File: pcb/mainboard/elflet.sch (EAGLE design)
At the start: 37 parts, among them J1 ZX62-B-5PA(33), J2 2212S-10SG-36, J3 STD-PINHD-1X6, Q1 IRLML6344TRPBF, Q2 ALS-PT19-315C/L177/TR8, SW1 SKRPACE010, U1 ESP-WROOM-32, U2 ADP3338AKCZ-3.3, U3 OSRB38C9AA, U4 BME280

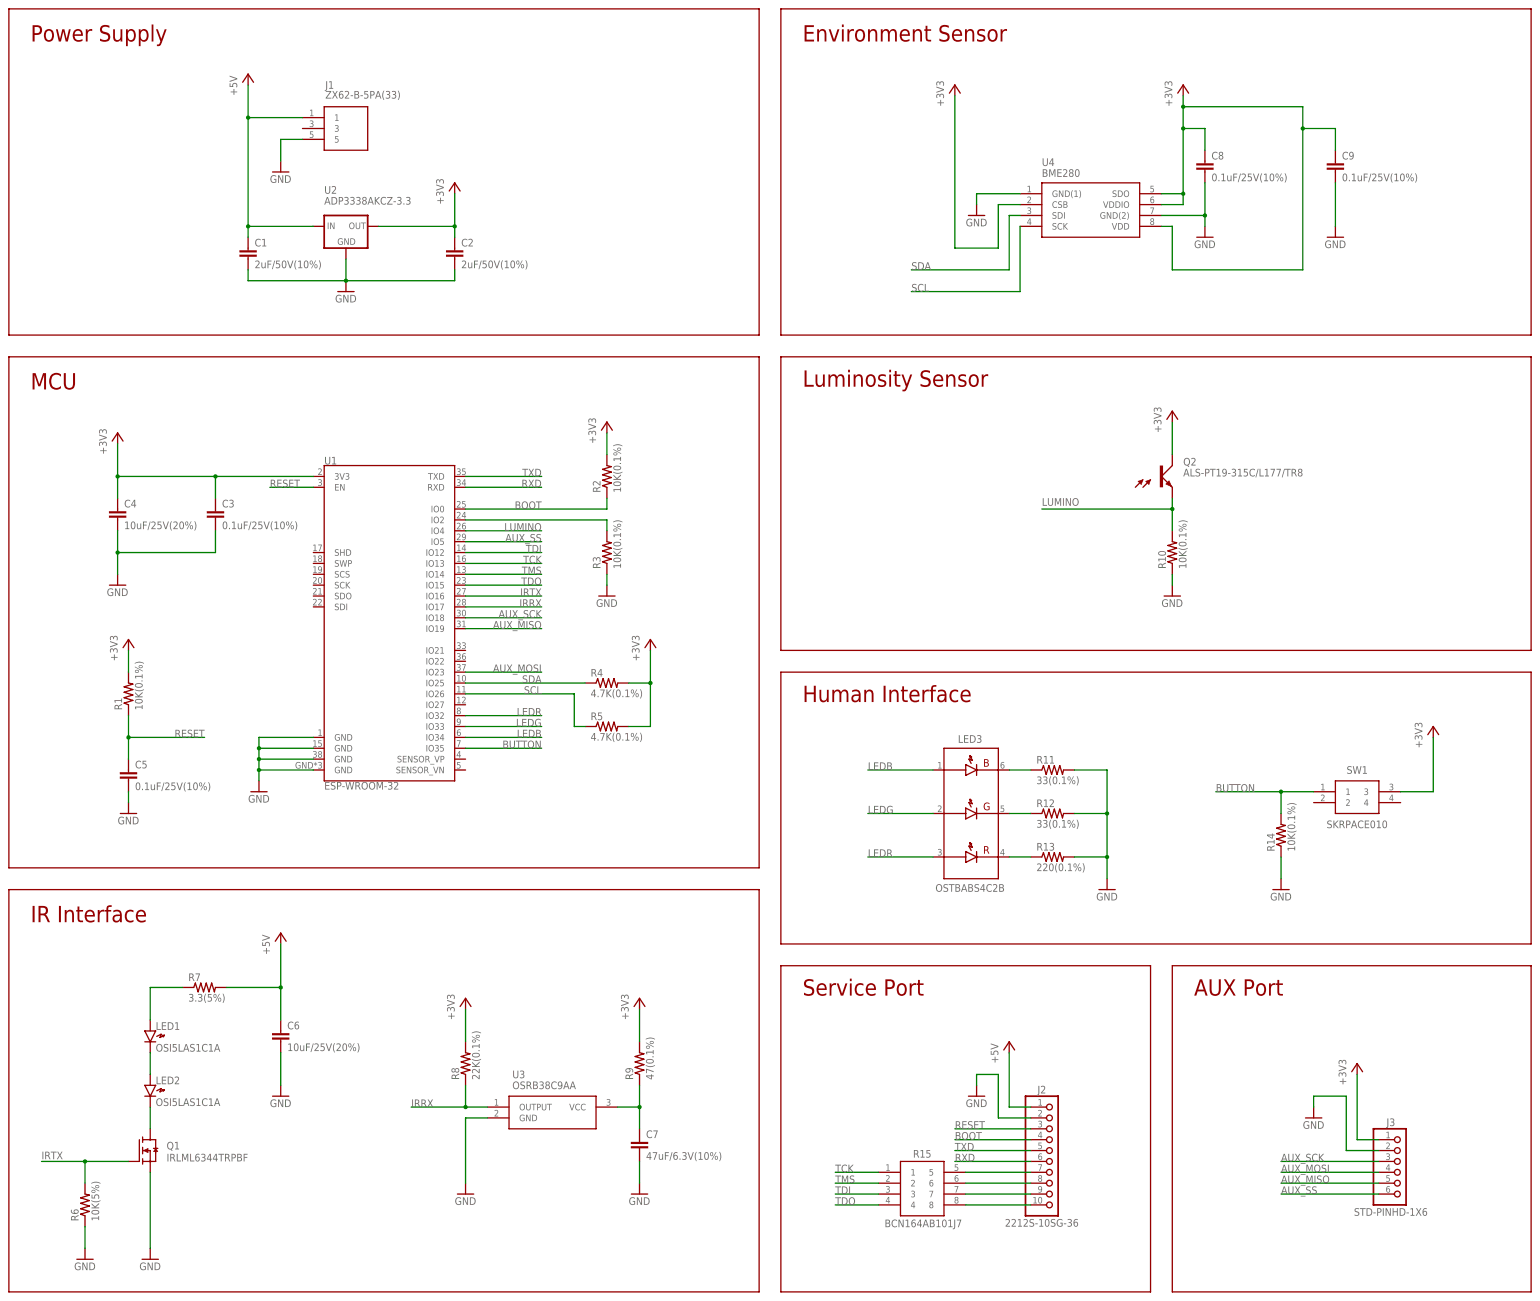
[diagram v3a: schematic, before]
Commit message: fix usb connector issue
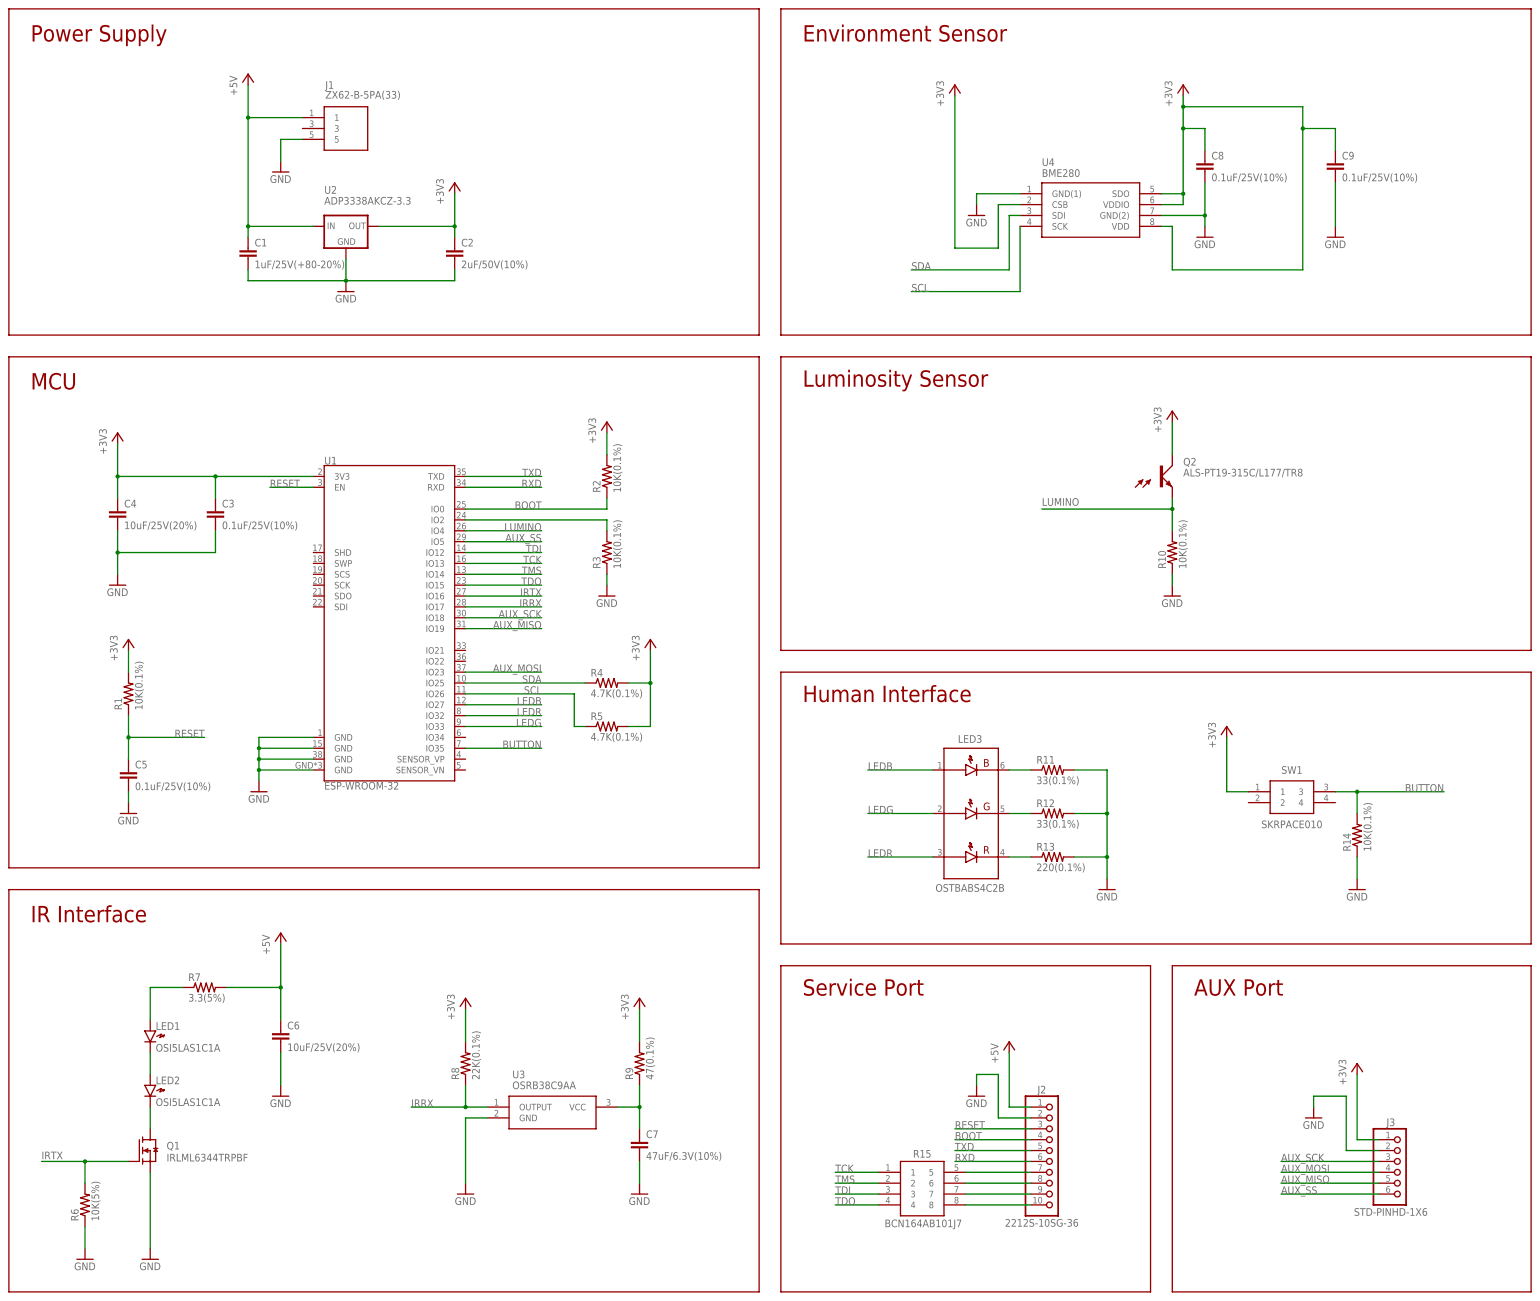
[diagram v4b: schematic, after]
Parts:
- C1: value 2uF/50V(10%) -> 1uF/25V(+80-20%)
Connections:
- net +3V3: now also SW1.1; no longer SW1.3
- net BUTTON: now also SW1.3; no longer SW1.1
- net LEDB: now also U1.IO27; no longer U1.IO34
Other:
- moved on the sheet: R14, SW1
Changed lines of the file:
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@@
 <part name="GND1" library="supply1" library_urn="urn:adsk.eagle:library:371" deviceset="GND" device=""/>
 <part name="GND2" library="supply1" library_urn="urn:adsk.eagle:library:371" deviceset="GND" device=""/>
-<part name="C1" library="rcl" library_urn="urn:adsk.eagle:library:334" deviceset="C-EU" device="C3216" package3d_urn="urn:adsk.eagle:package:23628/2" value="2uF/50V(10%)"/>
+<part name="C1" library="rcl" library_urn="urn:adsk.eagle:library:334" deviceset="C-EU" device="C3216" package3d_urn="urn:adsk.eagle:package:23628/2" value="1uF/25V(+80-20%)"/>
 <part name="C2" library="rcl" library_urn="urn:adsk.eagle:library:334" deviceset="C-EU" device="C3216" package3d_urn="urn:adsk.eagle:package:23628/2" value="2uF/50V(10%)"/>
 <part name="+3V1" library="supply1" library_urn="urn:adsk.eagle:library:371" deviceset="+3V3" device=""/>
@@
 <instance part="R13" gate="G$1" x="243.84" y="101.6"/>
 <instance part="GND17" gate="1" x="256.54" y="93.98"/>
-<instance part="SW1" gate="G$1" x="304.8" y="116.84"/>
-<instance part="+3V11" gate="G$1" x="332.74" y="132.08"/>
-<instance part="R14" gate="G$1" x="297.18" y="106.68" rot="R90"/>
-<instance part="GND18" gate="1" x="297.18" y="93.98"/>
+<instance part="SW1" gate="G$1" x="289.56" y="116.84"/>
+<instance part="+3V11" gate="G$1" x="284.48" y="132.08"/>
+<instance part="R14" gate="G$1" x="314.96" y="106.68" rot="R90"/>
+<instance part="GND18" gate="1" x="314.96" y="93.98"/>
 <instance part="J2" gate="G$1" x="246.38" y="35.56"/>
 <instance part="GND6" gate="1" x="226.06" y="45.72"/>
@@
 <pinref part="R14" gate="G$1" pin="1"/>
 <pinref part="GND18" gate="1" pin="GND"/>
-<wire x1="297.18" y1="101.6" x2="297.18" y2="96.52" width="0.1524" layer="91"/>
+<wire x1="314.96" y1="101.6" x2="314.96" y2="96.52" width="0.1524" layer="91"/>
 </segment>
 <segment>
@@
 </segment>
 <segment>
-<pinref part="+3V11" gate="G$1" pin="+3V3"/>
-<pinref part="SW1" gate="G$1" pin="3"/>
-<wire x1="332.74" y1="129.54" x2="332.74" y2="116.84" width="0.1524" layer="91"/>
-<wire x1="332.74" y1="116.84" x2="325.12" y2="116.84" width="0.1524" layer="91"/>
-</segment>
-<segment>
 <pinref part="J3" gate="G$1" pin="1"/>
 <wire x1="320.04" y1="35.56" x2="314.96" y2="35.56" width="0.1524" layer="91"/>
 <pinref part="+3V13" gate="G$1" pin="+3V3"/>
 <wire x1="314.96" y1="35.56" x2="314.96" y2="50.8" width="0.1524" layer="91"/>
+</segment>
+<segment>
+<pinref part="SW1" gate="G$1" pin="1"/>
+<pinref part="+3V11" gate="G$1" pin="+3V3"/>
+<wire x1="289.56" y1="116.84" x2="284.48" y2="116.84" width="0.1524" layer="91"/>
+<wire x1="284.48" y1="116.84" x2="284.48" y2="129.54" width="0.1524" layer="91"/>
 </segment>
 </net>
@@
 </segment>
 <segment>
-<pinref part="SW1" gate="G$1" pin="1"/>
-<label x="281.94" y="116.84" size="1.778" layer="95"/>
-<wire x1="304.8" y1="116.84" x2="297.18" y2="116.84" width="0.1524" layer="91"/>
+<pinref part="SW1" gate="G$1" pin="3"/>
+<wire x1="309.88" y1="116.84" x2="314.96" y2="116.84" width="0.1524" layer="91"/>
 <pinref part="R14" gate="G$1" pin="2"/>
-<wire x1="297.18" y1="116.84" x2="281.94" y2="116.84" width="0.1524" layer="91"/>
-<wire x1="297.18" y1="111.76" x2="297.18" y2="116.84" width="0.1524" layer="91"/>
-<junction x="297.18" y="116.84"/>
+<wire x1="314.96" y1="116.84" x2="335.28" y2="116.84" width="0.1524" layer="91"/>
+<wire x1="314.96" y1="111.76" x2="314.96" y2="116.84" width="0.1524" layer="91"/>
+<junction x="314.96" y="116.84"/>
+<label x="335.28" y="116.84" size="1.778" layer="95" rot="MR0"/>
 </segment>
 </net>
 <net name="LEDB" class="0">
-<segment>
-<pinref part="U1" gate="G$1" pin="IO34"/>
-<wire x1="106.68" y1="129.54" x2="124.46" y2="129.54" width="0.1524" layer="91"/>
-<label x="124.46" y="129.54" size="1.778" layer="95" rot="MR0"/>
-</segment>
 <segment>
 <pinref part="LED3" gate="G$1" pin="AB"/>
@@
 <label x="200.66" y="121.92" size="1.778" layer="95"/>
 </segment>
-</net>
+<segment>
+<pinref part="U1" gate="G$1" pin="IO27"/>
+<wire x1="106.68" y1="137.16" x2="124.46" y2="137.16" width="0.1524" layer="91"/>
+<label x="124.46" y="137.16" size="1.778" layer="95" rot="MR0"/>
+</segment>
+</net>
